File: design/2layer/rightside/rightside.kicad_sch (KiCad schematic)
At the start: 233 parts, among them IC2 MCP23009-E_MG, IC3 nRF52833-QDAA-R7, IC5 XCL110A503KR-G, IC6 TPS22917LDBVT, IC7 SN74AHCT1G125DCKR, IC8 TPS63051RMWT, J1 USB_C_Receptacle_USB2.0_16P, J2 Battery+, J3 Battery-, J4 OLED_128x32, J5 Conn_01x01, J6 Conn_01x04, J7 F32Q-1A7H1-11012, J8 Conn_01x01, U1 BQ27441-G1, U2 BQ24072RGT, U3 USB6B1, U5 PEC11L-4015F-S0015, Y1 ECS-320-8-37B2-JTY-TR

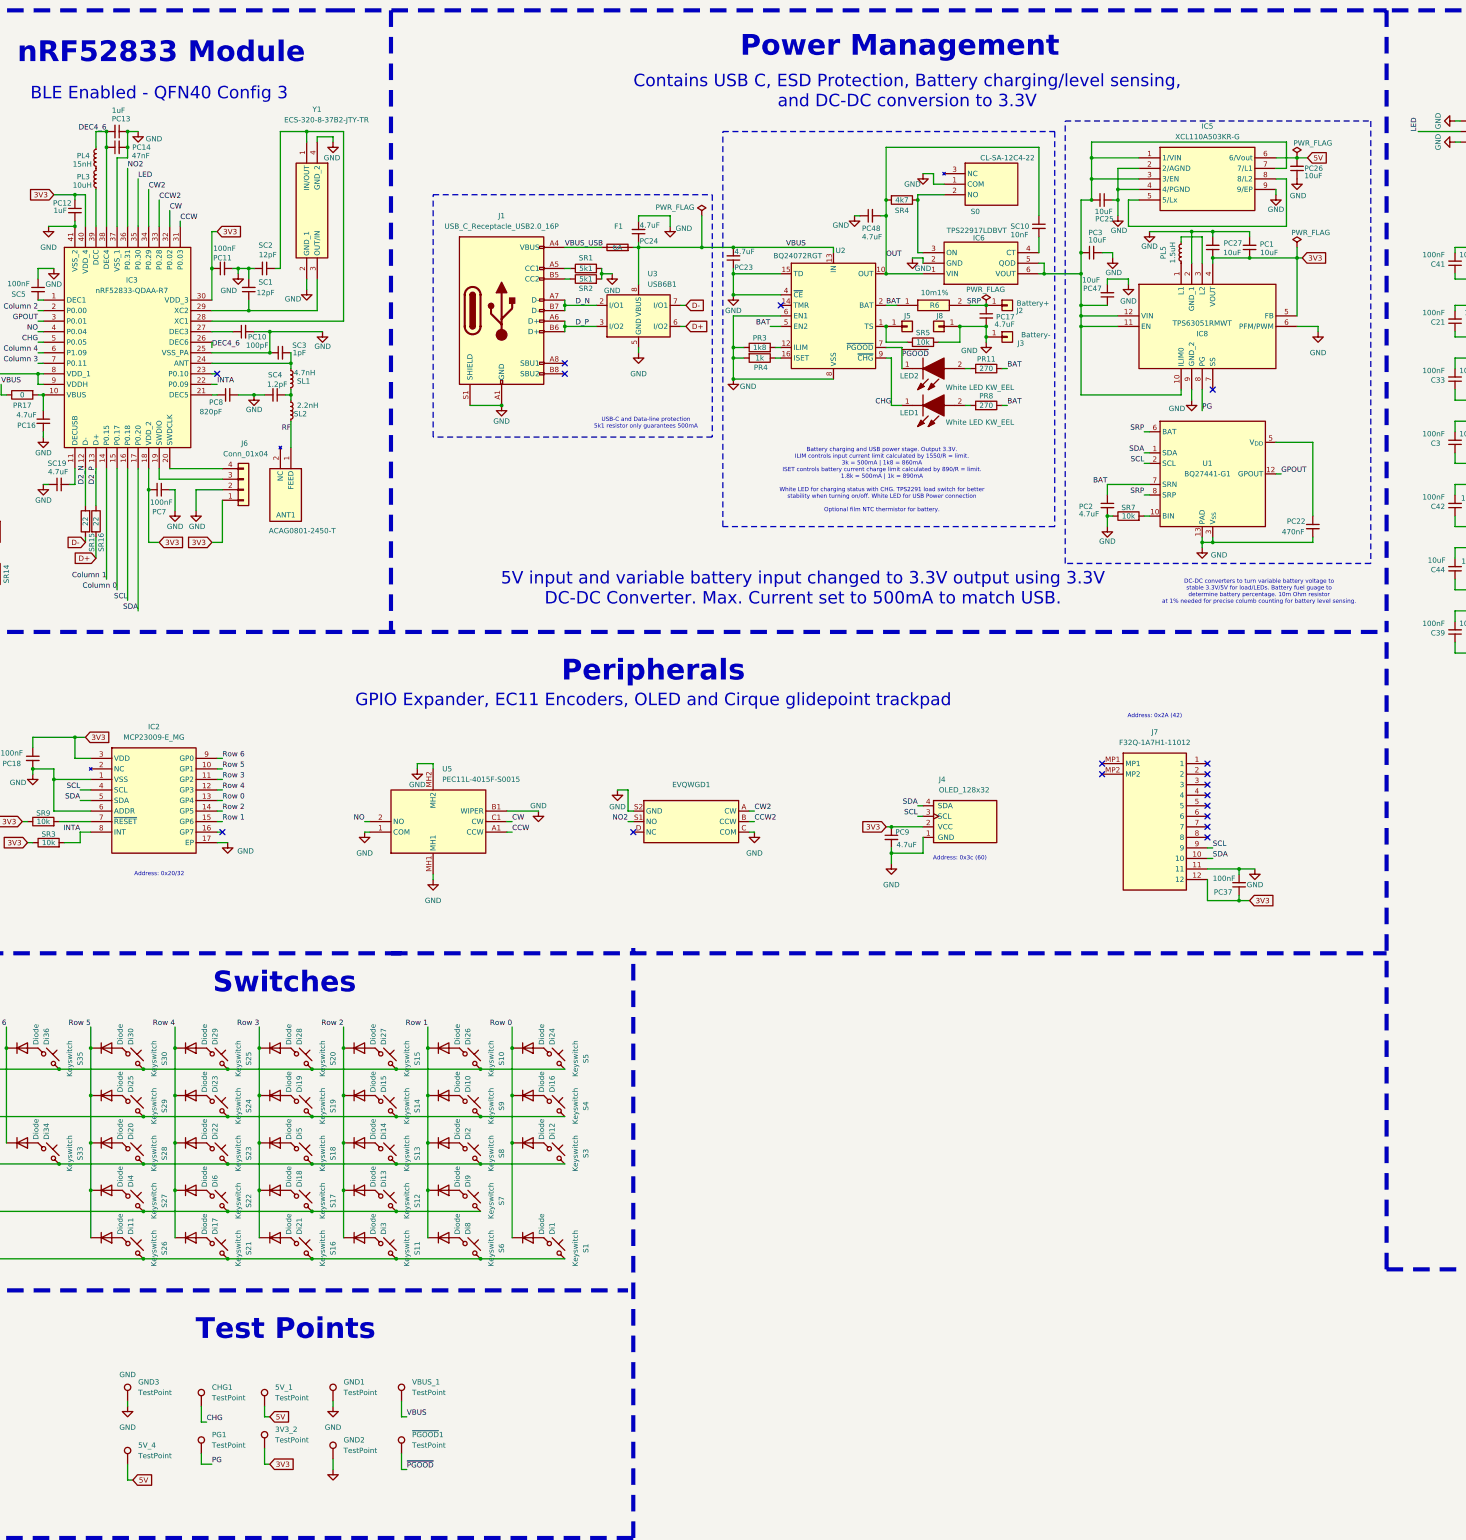
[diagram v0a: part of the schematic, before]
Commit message: Replaced TPS63051 with TPS63031 as out of stock
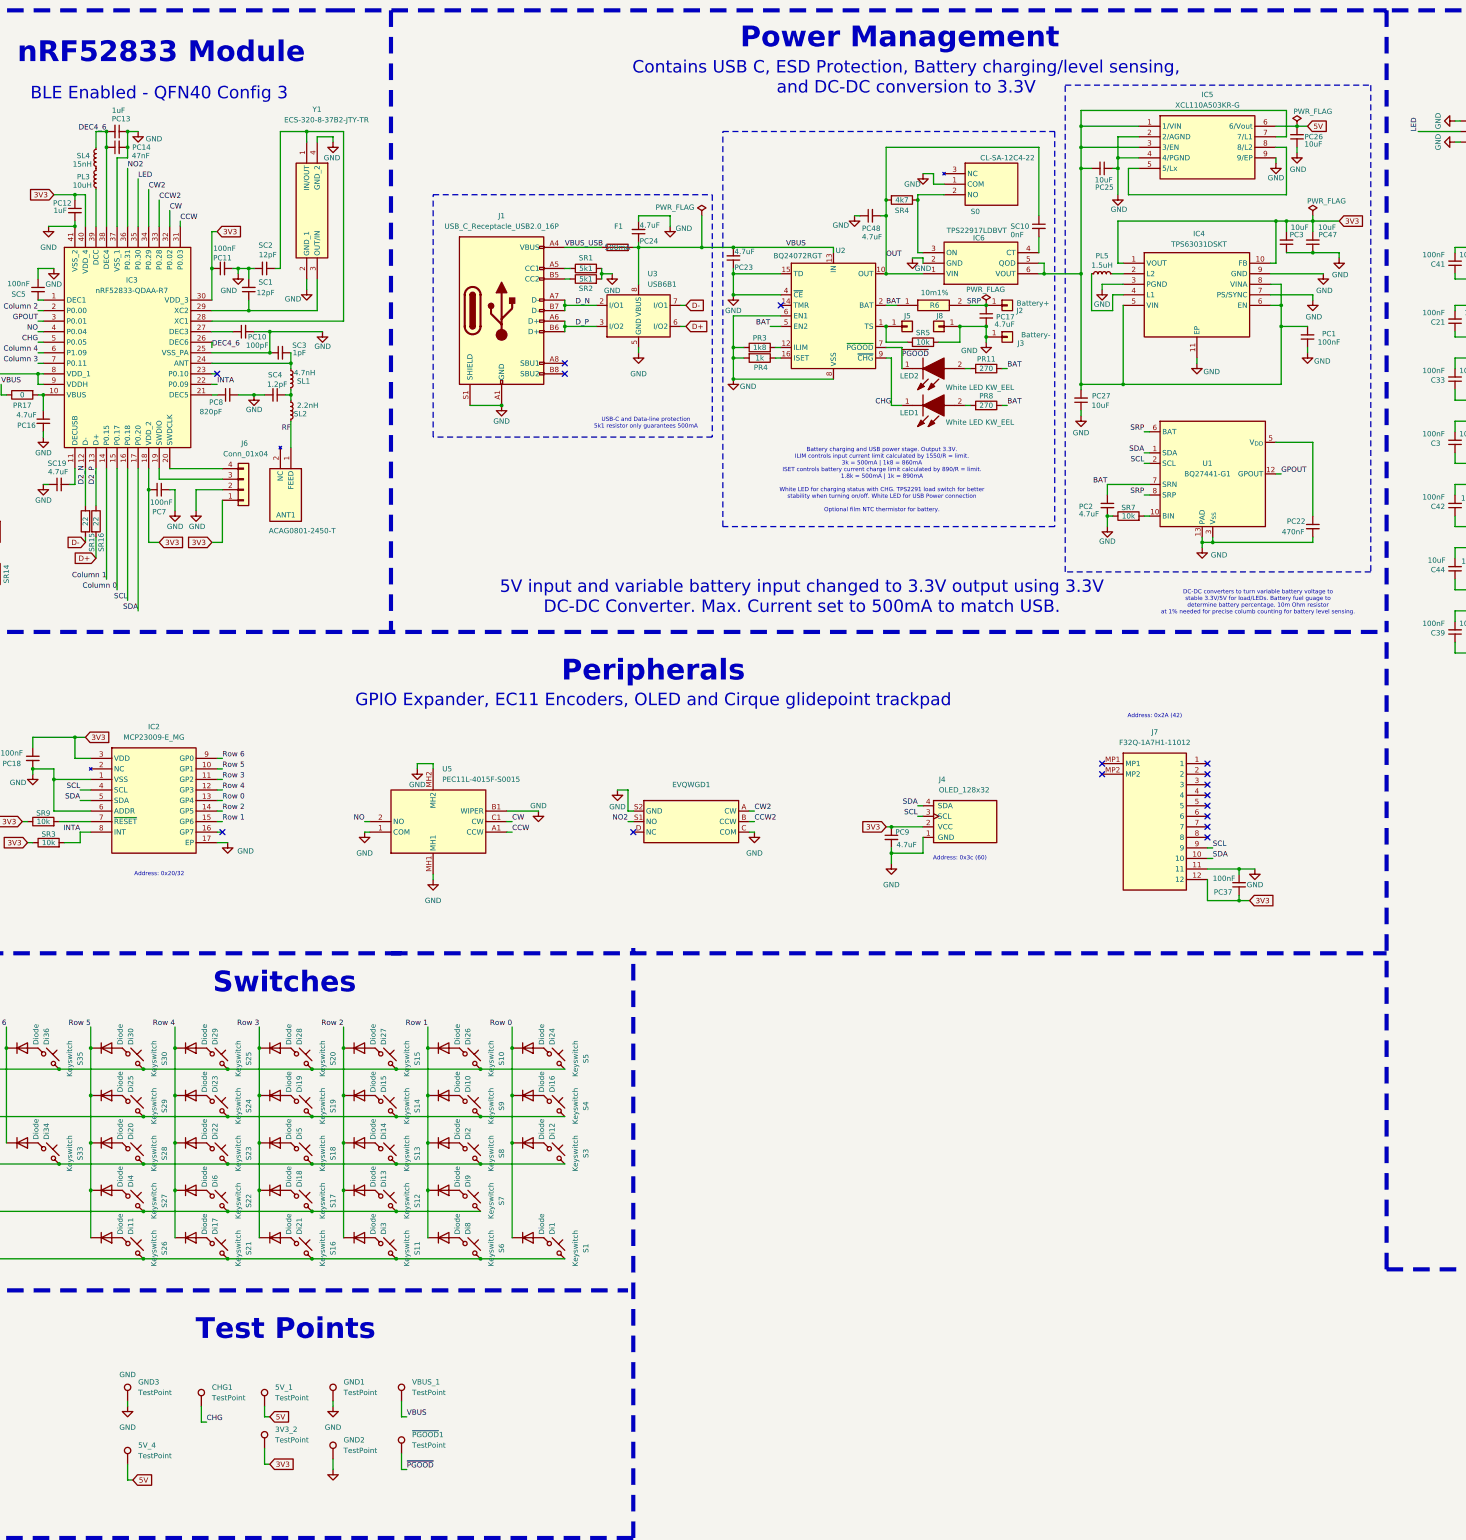
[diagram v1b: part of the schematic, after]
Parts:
- removed IC8: TPS63051RMWT, QFN50P250X250X100-12N-D, symbol SamacSys:TPS63051RMWT
- removed PG1: TestPoint, TestPoint:TestPoint_Pad_D1.0mm, symbol Connector:TestPoint
- added IC4: TPS63031DSKT, SON50P250X250X80-11N-D, symbol SamacSys:TPS63031DSKT
- F1: value 6A -> 500mA
- PC1: value 10uF -> 100nF
- SC10: value 10nF -> 0nF
- renumbered PL4 to SL4
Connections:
- net 3V3: now also PC3.2, PC47.2, IC4.1 (VOUT), IC4.10 (FB); no longer PC1.1, PC27.1
- net GND: now also PC1.1, PC27.1, PC3.1, PC47.1, IC4.11 (EP), IC4.3 (PGND), IC4.7 (PS/SYNC), IC4.9 (GND); no longer PC1.2, PC27.2, PC3.2, PC47.2
- net at IC5.1 (1/VIN), IC5.3 (3/EN), IC5.7 (7/L1)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: now also PC1.2, PC27.2, IC4.5 (VIN), IC4.6 (EN), IC4.8 (VINA); no longer PC3.1, PC47.1
- net at PL5.2: now also IC4.2 (L2)
- net at PL5.1: now also IC4.4 (L1)
- no-connect marks 18 -> 17
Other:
- moved on the sheet: IC5, PC1, PC25, PC26, PC3, PC47, PL5

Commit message: Create blender model + PCB review fixes
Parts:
- removed C29, C39, C4, C45: 100nF, ScottoKeebs_Components:Capacitor_0603, symbol Device:C_Small
- removed C44: 10uF, ScottoKeebs_Components:Capacitor_0603, symbol Device:C_Small
- removed PL5: 1.5uH, Inductor_SMD:L_0603_1608Metric, symbol Device:L_Small
- added C46, PC28: 100nF, ScottoKeebs_Components:Capacitor_0603, symbol Device:C_Small
- added PC29: 10uF, ScottoKeebs_Components:Capacitor_0603, symbol Device:C_Small
- added PL1: LPS3015-153MRC, Snapeda:IND_LPS3015-153MRC, symbol Device:L
- added SR17, SR18: 47, Resistor_SMD:R_0603_1608Metric, symbol Device:R
- added SR6: 100k, Resistor_SMD:R_0603_1608Metric, symbol Device:R
- C2, C21, C28, C3, C30, C31, C32, C33, C35, C36, C38, C41, C42, C43: value 100nF -> 10uF
- F1: value 500mA -> .75A
- PR3: value 1k8 -> 2k2
- SC10: value 0nF -> 0nF(10)
- SR4: value 4k7 -> 100k
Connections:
- net 5V: now also C46.1, PC29.2
- net GND: now also C46.2, PC28.2, PC29.1, SR6.1
- net Row 0: now also Di1.2 (A), Di12.2 (A), Di16.2 (A), Di24.2 (A), IC2.14 (GP5); no longer Di1.1 (K), Di12.1 (K), Di16.1 (K), Di24.1 (K), IC2.13 (GP4)
- net Row 1: now also Di10.2 (A), Di2.2 (A), Di26.2 (A), Di8.2 (A), Di9.2 (A), IC2.16 (GP7); no longer Di10.1 (K), Di2.1 (K), Di26.1 (K), Di8.1 (K), Di9.1 (K), IC2.15 (GP6)
- net Row 2: now also Di13.2 (A), Di14.2 (A), Di15.2 (A), Di27.2 (A), Di3.2 (A), IC2.15 (GP6); no longer Di13.1 (K), Di14.1 (K), Di15.1 (K), Di27.1 (K), Di3.1 (K), IC2.14 (GP5)
- net Row 3: now also Di18.2 (A), Di19.2 (A), Di21.2 (A), Di28.2 (A), Di5.2 (A), IC2.12 (GP3); no longer Di18.1 (K), Di19.1 (K), Di21.1 (K), Di28.1 (K), Di5.1 (K), IC2.11 (GP2)
- net Row 4: now also Di17.2 (A), Di22.2 (A), Di23.2 (A), Di29.2 (A), Di6.2 (A), IC2.13 (GP4); no longer Di17.1 (K), Di22.1 (K), Di23.1 (K), Di29.1 (K), Di6.1 (K), IC2.12 (GP3)
- net Row 5: now also Di11.2 (A), Di20.2 (A), Di25.2 (A), Di30.2 (A), Di4.2 (A), IC2.11 (GP2); no longer Di11.1 (K), Di20.1 (K), Di25.1 (K), Di30.1 (K), Di4.1 (K), IC2.10 (GP1)
- net Row 6: now also Di34.2 (A), Di36.2 (A); no longer Di34.1 (K), Di36.1 (K)
- net SCL: now also SR17.1; no longer IC3.16 (P0.18)
- net SDA: now also SR18.2; no longer IC3.17 (P0.20)
- net VBUS: now also PC28.1
- net at S4.2: now also Di16.1 (K); no longer Di16.2 (A)
- net at S11.2: now also Di3.1 (K); no longer Di3.2 (A)
- net at S33.2: now also Di34.1 (K); no longer Di34.2 (A)
- net at IC4.5 (VIN), IC4.6 (EN), IC4.8 (VINA)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: no longer IC5.3 (3/EN)
- net at S22.2: now also Di6.1 (K); no longer Di6.2 (A)
- net at S6.2: now also Di8.1 (K); no longer Di8.2 (A)
- net at S23.2: now also Di22.1 (K); no longer Di22.2 (A)
- net at S19.2: now also Di19.1 (K); no longer Di19.2 (A)
- net at S8.2: now also Di2.1 (K); no longer Di2.2 (A)
- net at S17.2: now also Di18.1 (K); no longer Di18.2 (A)
- net at S26.2: now also Di11.1 (K); no longer Di11.2 (A)
- net at S35.2: now also Di36.1 (K); no longer Di36.2 (A)
- net at S29.2: now also Di25.1 (K); no longer Di25.2 (A)
- net at S14.2: now also Di15.1 (K); no longer Di15.2 (A)
- net at S13.2: now also Di14.1 (K); no longer Di14.2 (A)
- net at S24.2: now also Di23.1 (K); no longer Di23.2 (A)
- net at S3.2: now also Di12.1 (K); no longer Di12.2 (A)
- net at S28.2: now also Di20.1 (K); no longer Di20.2 (A)
- net at S9.2: now also Di10.1 (K); no longer Di10.2 (A)
- net at S30.2: now also Di30.1 (K); no longer Di30.2 (A)
- net at S1.2: now also Di1.1 (K); no longer Di1.2 (A)
- net at S10.2: now also Di26.1 (K); no longer Di26.2 (A)
- net at S12.2: now also Di13.1 (K); no longer Di13.2 (A)
- net at S25.2: now also Di29.1 (K); no longer Di29.2 (A)
- net at IC4.4 (L1): now also PL1.1
- net at IC4.2 (L2): now also PL1.2
- net at S18.2: now also Di5.1 (K); no longer Di5.2 (A)
- net at S5.2: now also Di24.1 (K); no longer Di24.2 (A)
- net at S7.2: now also Di9.1 (K); no longer Di9.2 (A)
- net at S20.2: now also Di28.1 (K); no longer Di28.2 (A)
- net at S27.2: now also Di4.1 (K); no longer Di4.2 (A)
- net at S15.2: now also Di27.1 (K); no longer Di27.2 (A)
- net at S21.2: now also Di17.1 (K); no longer Di17.2 (A)
- net at S16.2: now also Di21.1 (K); no longer Di21.2 (A)
- new net: IC3.16 (P0.18), SR17.2
- new net: IC3.17 (P0.20), SR18.1
- new net 5VEN: IC2.10 (GP1), IC5.3 (3/EN), SR6.2
- no-connect marks 17 -> 16
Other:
- note added: "Address: 0x55 (85)"
- note added: "BLE Enabled - QFN40 Config 5"
- note added: "Battery charging and USB power stage. ILIM controls input current limit calculated by 1550/R = limit. 3k = 500mA | 2k2 = 705mA ISET controls battery current charge limit calculated by 890/R = limit. 1.8k = 500mA | 1k = 890mA White LED for charging status with CHG. TPS2291 load switch for better stability when turning on/off. White LED for USB Power connection Optional film NTC thermistor for batt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"
- note removed: "BLE Enabled - QFN40 Config 3"
- note removed: "Battery charging and USB power stage. Output 3.3V. ILIM controls input current limit calculated by 1550/R = limit. 3k = 500mA | 1k8 = 860mA ISET controls battery current charge limit calculated by 890/R = limit. 1.8k = 500mA | 1k = 890mA White LED for charging status with CHG. TPS2291 load switch for better stability when turning on/off. White LED for USB Power connection Optional film NTC thermi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"
- moved on the sheet: Di1, Di10, Di11, Di12, Di13, Di14, Di15, Di16, Di17, Di18, Di19, Di2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
